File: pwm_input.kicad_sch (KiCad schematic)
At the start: 0 parts

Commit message: chore: update KiCad project settings and sync internal revision history
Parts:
- added J5: Fan_4pin, connectors:0470531000, symbol connectors:Fan_4pin
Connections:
- new net +12V: J5.2 (+12V)
- new net GND: J5.1 (GND)
- new net PWM_input: J5.4 (PWM)

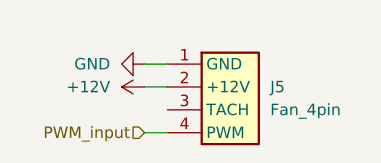
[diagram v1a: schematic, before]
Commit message: feat: add Mol connectors and update schematic and PCB designs
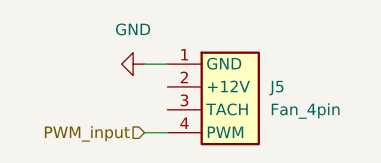
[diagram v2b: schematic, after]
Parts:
- J5: footprint connectors:0470531000 -> connectors:CONN_SD-47053-001_H10p00_MOL
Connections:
- net +12V: no longer names the net of J5.2 (+12V)
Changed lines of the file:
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@@
 	(wire
 		(pts
-			(xy 63.5 39.37) (xy 66.04 39.37)
+			(xy 63.5 36.83) (xy 66.04 36.83)
 		)
 		(stroke
@@
 		)
 	)
-	(wire
-		(pts
-			(xy 63.5 36.83) (xy 66.04 36.83)
-		)
-		(stroke
-			(width 0)
-			(type default)
-		)
-	)
 	(hierarchical_label "PWM_input"
 		(shape input)
@@
 			)
 			(justify right)
-		)
-	)
-	(symbol
-		(lib_id "power:+12V")
-		(at 63.5 39.37 90)
-		(unit 1)
-		(body_style 1)
-		(exclude_from_sim no)
-		(in_bom yes)
-		(on_board yes)
-		(in_pos_files yes)
-		(dnp no)
-		(fields_autoplaced yes)
-		(property "Reference" "#PWR011"
-			(at 67.31 39.37 0)
-			(hide yes)
-			(show_name no)
-			(do_not_autoplace no)
-			(effects
-				(font
-					(size 1.27 1.27)
-				)
-			)
-		)
-		(property "Value" "+12V"
-			(at 59.69 39.3699 90)
-			(show_name no)
-			(do_not_autoplace no)
-			(effects
-				(font
-					(size 1.27 1.27)
-				)
-				(justify left)
-			)
-		)
-		(property "Footprint" ""
-			(at 63.5 39.37 0)
-			(hide yes)
-			(show_name no)
-			(do_not_autoplace no)
-			(effects
-				(font
-					(size 1.27 1.27)
-				)
-			)
-		)
-		(property "Datasheet" ""
-			(at 63.5 39.37 0)
-			(hide yes)
-			(show_name no)
-			(do_not_autoplace no)
-			(effects
-				(font
-					(size 1.27 1.27)
-				)
-			)
-		)
-		(property "Description" "Power symbol creates a global label with name \"+12V\""
-			(at 63.5 39.37 0)
-			(hide yes)
-			(show_name no)
-			(do_not_autoplace no)
-			(effects
-				(font
-					(size 1.27 1.27)
-				)
-			)
-		)
-		(pin "1"
-		)
-		(instances
-			(project "12V_pwm_pump_and_fan_adaptor_board"
-				(path "/1e5bcf57-ecaf-4c00-86fd-4242d519fbb4/dfd25b30-7961-4c66-b5ae-73ff5417fe22"
-					(reference "#PWR011")
-					(unit 1)
-				)
-			)
 		)
 	)
@@
 			)
 		)
-		(property "Footprint" "connectors:0470531000"
+		(property "Footprint" "connectors:CONN_SD-47053-001_H10p00_MOL"
 			(at 71.12 49.53 0)
 			(hide yes)
@@
 		)
 		(property "Value" "GND"
-			(at 59.69 36.8299 90)
+			(at 62.23 33.02 90)
 			(show_name no)
 			(do_not_autoplace no)
@@
 					(size 1.27 1.27)
 				)
-				(justify right)
 			)
 		)
